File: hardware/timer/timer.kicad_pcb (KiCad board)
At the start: 2 copper layers, 80 x 80 mm, 22 parts, among them J1 JST_XH_HOST_UART, U1 Pico, U2 TM1637

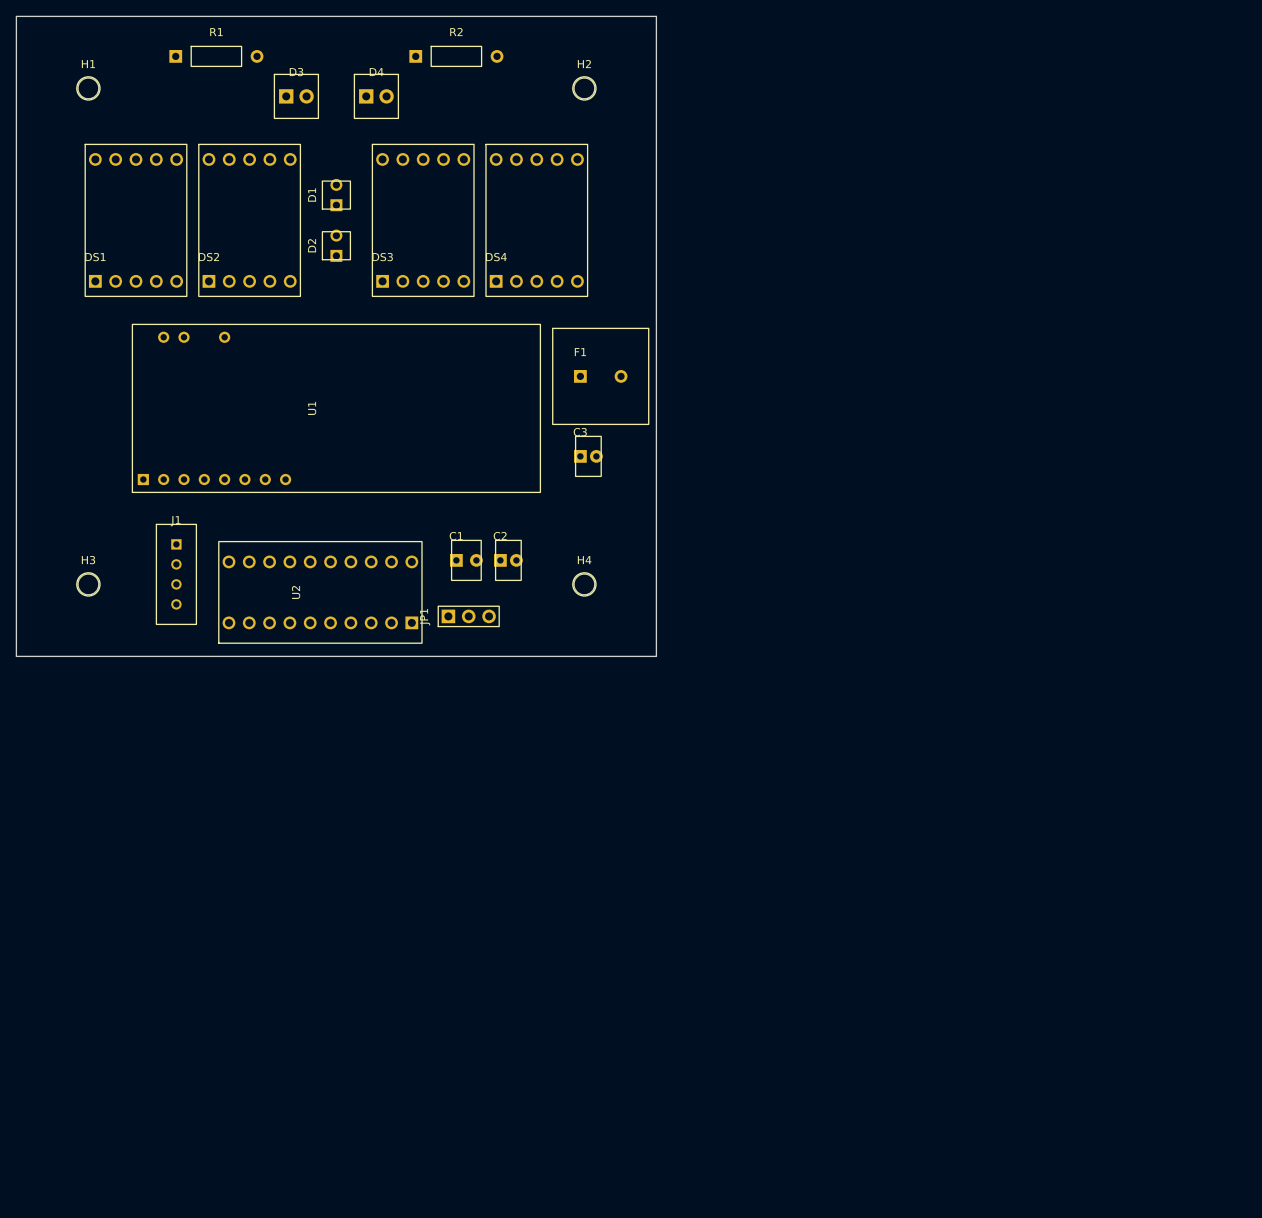
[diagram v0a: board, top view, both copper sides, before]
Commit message: タイマー基板: 実フットプリント化・電池入力(J6/Q1/R5)追加・Pico 40ピン化・配線
- PCBを実ライブラリのフットプリントで作り直し、以後KiCadで手編集(tools/に一回限りのスクリプト)
- 回路図のFootprintフィールドを補完、C3を8mm缶に変更
- Pico専用フットプリント RPi_Pico_TH_Headers(THT40ピンのみ、浮き実装、3D +2.5mm)と40ピンシンボル
- 電池入力 J6 -> Q1(逆接続保護) -> +5V。F6は廃止(保護は電池箱側)
- 未解決(作業途中): DRCのstarved_thermal 4件、回路図とのパリティ差分(基板更新で解消見込み)

Co-Authored-By: Claude Sonnet 5.5 <noreply@anthropic.com>
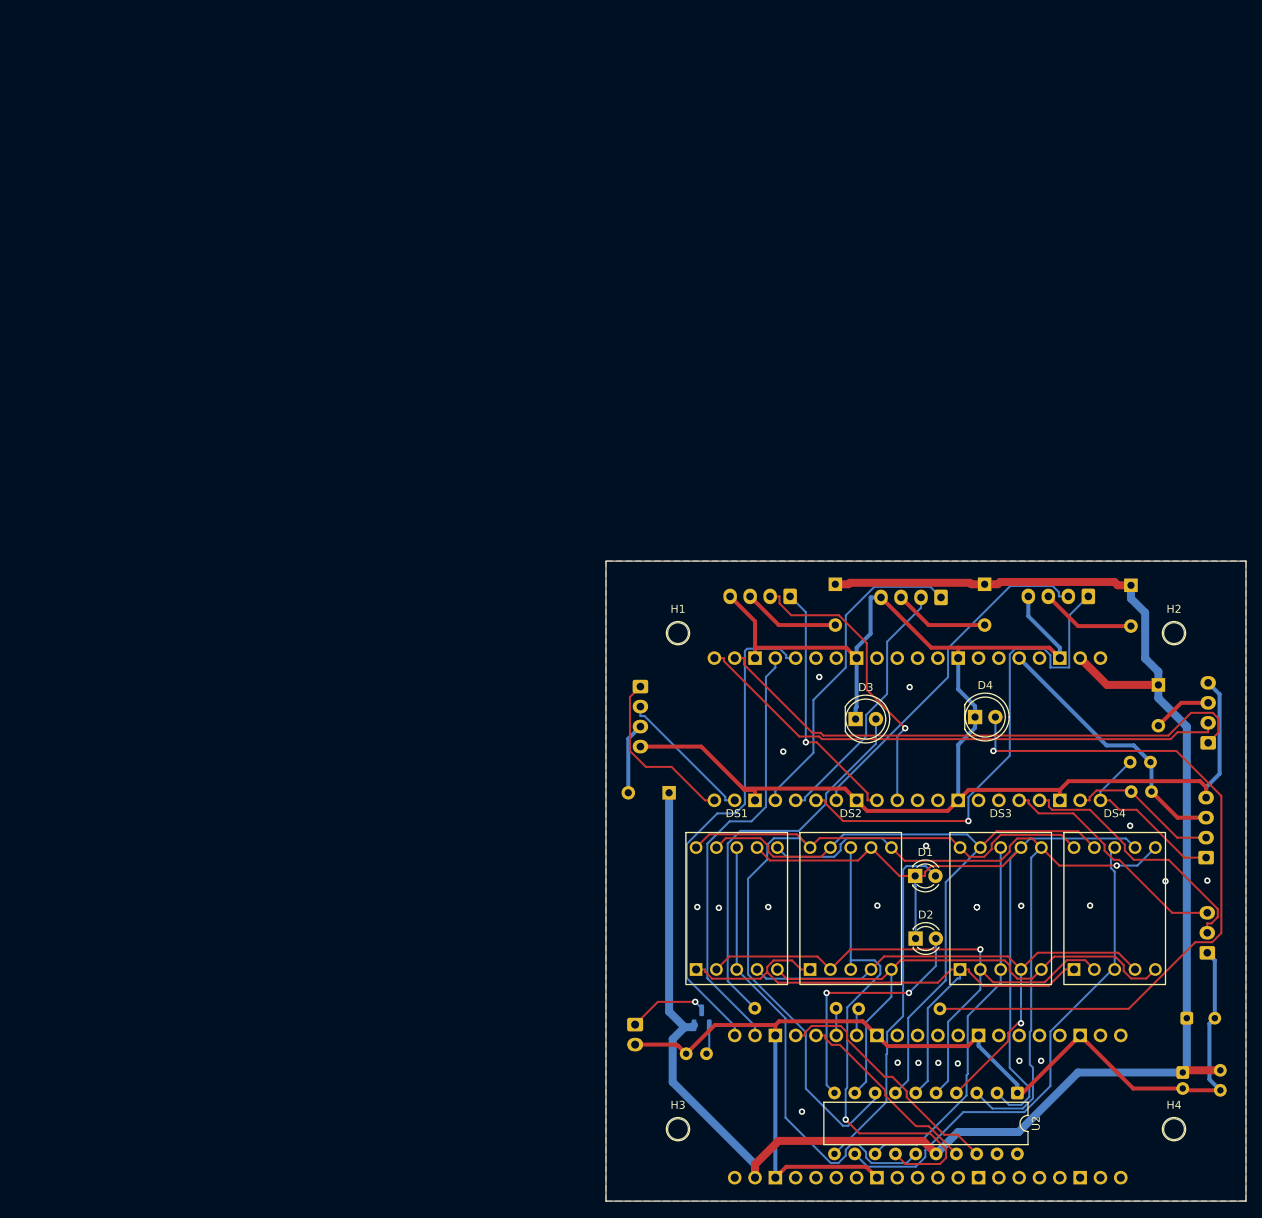
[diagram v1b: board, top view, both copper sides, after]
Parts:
- removed JP1: TM1637_VDD_SEL, Connector_PinHeader_2.54mm:PinHeader_1x03_P2.54mm_Vertical
- added F2: MF-RX030/72-0 (0.3A hold, Akizuki 113076), Timer_Local:MF-RX030_Radial_P5.10mm, B.Cu at (121.0, 71.0)
- added F3: MF-RX030/72-0 (0.3A hold, Akizuki 113076), Timer_Local:MF-RX030_Radial_P5.10mm, B.Cu at (139.3, 71.1)
- added F4: MF-RX030/72-0 (0.3A hold, Akizuki 113076), Timer_Local:MF-RX030_Radial_P5.10mm, B.Cu at (81.6, 97.0)
- added F5: MF-RX030/72-0 (0.3A hold, Akizuki 113076), Timer_Local:MF-RX030_Radial_P5.10mm, B.Cu at (142.7, 83.6)
- added J2: MODULE_SLOT_2, Connector_JST:JST_XH_B4B-XH-A_1x04_P2.50mm_Vertical, B.Cu at (115.6, 72.6)
- added J3: MODULE_SLOT_3, Connector_JST:JST_XH_B4B-XH-A_1x04_P2.50mm_Vertical, B.Cu at (134.0, 72.5)
- added J4: MODULE_SLOT_4, Connector_JST:JST_XH_B4B-XH-A_1x04_P2.50mm_Vertical, B.Cu at (78.0, 83.8)
- added J5: MODULE_SLOT_5, Connector_JST:JST_XH_B4B-XH-A_1x04_P2.50mm_Vertical, B.Cu at (149.0, 90.8)
- added J6: PWR_IN, Connector_JST:JST_XH_B2B-XH-A_1x02_P2.50mm_Vertical, B.Cu at (77.3, 126.0)
- added J7: SHARED_WIDGET_I2C_TAP, Connector_JST:JST_XH_B4B-XH-A_1x04_P2.50mm_Vertical, B.Cu at (148.7, 105.2)
- added J8: SHARED_WIDGET_GPIO, Connector_JST:JST_XH_B3B-XH-A_1x03_P2.50mm_Vertical, B.Cu at (148.9, 117.1)
- added Q1: IRLML6402, Package_TO_SOT_SMD:SOT-23, B.Cu at (85.7, 125.2)
- added R3: 4.7k, Resistor_THT:R_Axial_DIN0207_L6.3mm_D2.5mm_P2.54mm_Vertical, B.Cu at (141.8, 93.2)
- added R4: 4.7k, Resistor_THT:R_Axial_DIN0207_L6.3mm_D2.5mm_P2.54mm_Vertical, B.Cu at (141.9, 96.9)
- added R5: 100k, Resistor_THT:R_Axial_DIN0207_L6.3mm_D2.5mm_P2.54mm_Vertical, B.Cu at (86.3, 129.7)
- added U3: Pico 2 (host / communication), Timer_Local:RPi_Pico_TH_Headers, B.Cu at (111.4, 89.1)
- C1, C2, R1, R2: moved to B.Cu
- C3: value 100uF -> 470uF; footprint Capacitor_THT:CP_Radial_D5.0mm_P2.00mm -> Capacitor_THT:CP_Radial_D8.0mm_P3.50mm; moved to B.Cu
- D1: value LED -> LED (colon, top)
- D2: value LED -> LED (colon, bottom)
- D3: value LED -> LED (strike 1)
- D4: value LED -> LED (strike 2)
- F1: value MF-R185 -> MF-RX030/72-0 (0.3A hold, Akizuki 113076); footprint Fuse_THT:Fuse_Radial_D12.0mm_P5.08mm -> Timer_Local:MF-RX030_Radial_P5.10mm; moved to B.Cu
- J1: value JST_XH_HOST_UART -> MODULE_SLOT_1; moved to B.Cu
- U1: footprint RPi_Pico:RPi_Pico_SMD_TH -> Timer_Local:RPi_Pico_TH_Headers; moved to B.Cu
- U2: footprint Timer_Local:TM1637 -> Package_DIP:DIP-20_W7.62mm
- moved R1 142.0 mm to (102.5, 124.0), turned to 180 degrees
- moved R2 129.2 mm to (105.3, 124.1)
- moved C1 114.8 mm to (150.5, 131.7), turned to -90 degrees
- moved U1 114.4 mm to (113.9, 136.3), turned to -90 degrees
- moved DS2 114.2 mm to (99.2, 119.1)
- moved DS1 114.2 mm to (85.0, 119.1)
- moved D2 112.9 mm to (112.4, 115.3), turned to 0 degrees
- moved DS4 112.3 mm to (132.2, 119.1)
- moved DS3 112.3 mm to (118.0, 119.1)
- moved D1 111.7 mm to (112.3, 107.4), turned to 0 degrees
- moved D4 107.8 mm to (119.8, 87.6)
- moved U2 107.3 mm to (125.1, 134.6), turned to -90 degrees
- moved C2 106.6 mm to (145.8, 132.0), turned to -90 degrees
- moved D3 104.6 mm to (104.9, 87.8)
- moved C3 103.3 mm to (146.3, 125.2)
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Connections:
- net GRID_COLON1 renamed /GRID_COLON1
- net GRID_COLON2 renamed /GRID_COLON2
- net GRID_D1 renamed /GRID_D1
- net GRID_D2 renamed /GRID_D2
- net GRID_D3 renamed /GRID_D3
- net GRID_D4 renamed /GRID_D4
- net SEG_A renamed /SEG_A
- net SEG_B renamed /SEG_B
- net SEG_C renamed /SEG_C
- net SEG_D renamed /SEG_D
- net SEG_DP renamed /SEG_DP
- net SEG_E renamed /SEG_E
- net SEG_F renamed /SEG_F
- net SEG_G renamed /SEG_G
- net STRIKE1 renamed /STRIKE1
- net STRIKE1_LED renamed /STRIKE1_LED
- net STRIKE2 renamed /STRIKE2
- net STRIKE2_LED renamed /STRIKE2_LED
- net TM_CLK renamed /TM_CLK
- net TM_DIO renamed /TM_DIO
- C1 pad 1: TM_VDD -> +5V
- C2 pad 1: TM_VDD -> +5V
- C3 pad 1: J1_5V -> +5V
- F1 pad 2: J1_5V -> /VCC_J1
- J1 pad 1: UART_TX -> /S1_RX
- J1 pad 2: UART_RX -> /S1_TX
- J1 pad 3: J1_5V -> /VCC_J1
- U1 pad 1: UART_TX -> /M_RX
- U1 pad 2: UART_RX -> /M_TX
- U1 pad 36: +3V3 -> +3.3V
- U2 pad 16: TM_VDD -> +5V
- U2 pad 19: (no net) -> unconnected-(U2-K1-Pad19)
- U2 pad 20: (no net) -> unconnected-(U2-K2-Pad20)
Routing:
- net GND: track 0.00 -> 330.9 mm, vias 0 -> 21
- net +5V: track 0.00 -> 233.7 mm
- net /SEG_G: track 0.00 -> 105.6 mm
- net /SEG_A: track 0.00 -> 98.4 mm
- net /SEG_B: track 0.00 -> 94.7 mm, vias 0 -> 1
- net /STRIKE2_LED: track 0.00 -> 91.9 mm, vias 0 -> 1
- net /SEG_F: track 0.00 -> 87.7 mm
- net /SEG_E: track 0.00 -> 76.0 mm
- net /SEG_D: track 0.00 -> 72.2 mm, vias 0 -> 1
- net /SEG_DP: track 0.00 -> 70.6 mm
- net /SEG_C: track 0.00 -> 70.3 mm, vias 0 -> 1
- net /S5_RX: track 0.00 -> 70.0 mm
- net /S5_TX: track 0.00 -> 67.7 mm
- net /GRID_D4: track 0.00 -> 63.5 mm
- net /S3_RX: track 0.00 -> 62.8 mm, vias 0 -> 1
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- added copper zone on B.Cu, net GND
- added copper zone on F.Cu, net GND
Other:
- board text added: "PROVISIONAL: 80x80mm, two Pico 2 (U1 timer, U3 host), dual-sided: front = display + Picos (pin-header mounted), back = JST/fuses/TM1637/passives; 4x M2.6 holes (9mm inset); dashed 12mm squares = corner keep-out (hub 2026-09-29)"
- board text removed: "PROVISIONAL: 80x80mm outline; 4x M2.6 mounting holes placed per 2026-09-29 hub decision (dia 2.6mm, 9mm inset from edge); dashed 15mm squares = corner keep-out (kept conservative pending screw head/washer confirmation)"

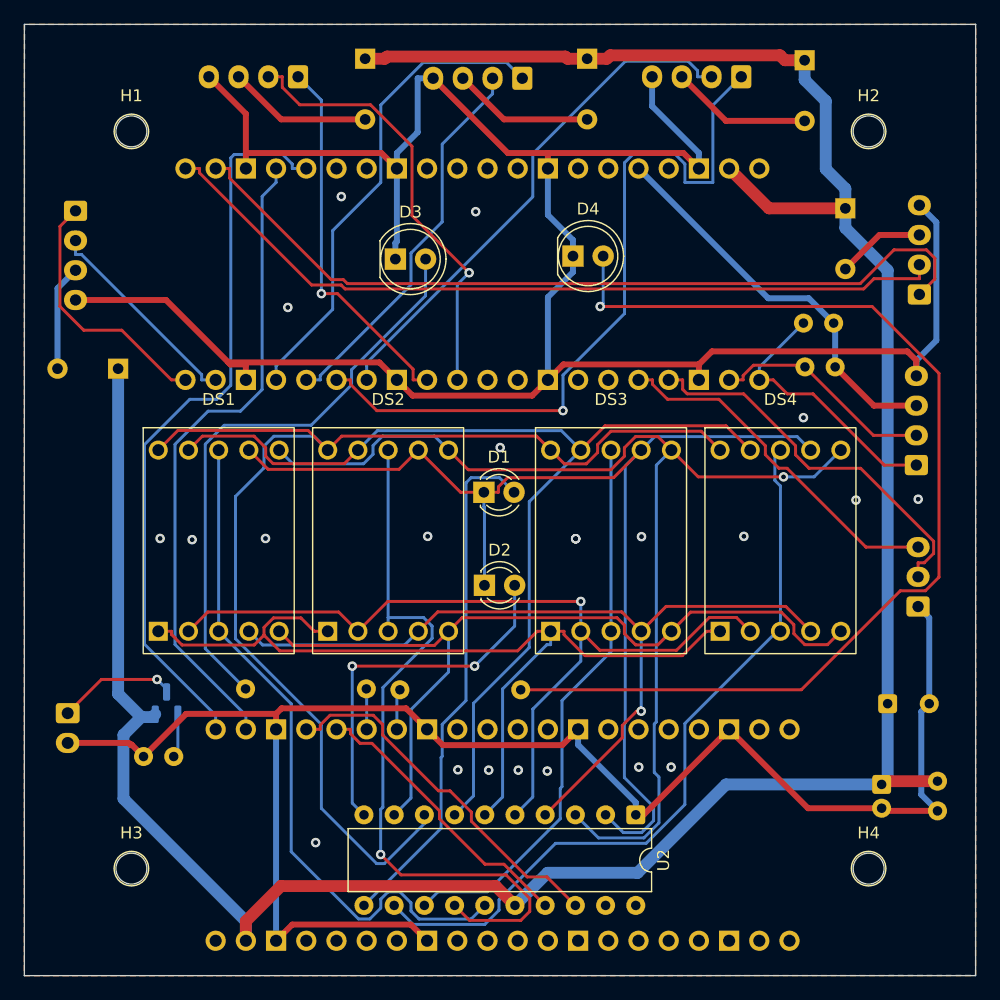
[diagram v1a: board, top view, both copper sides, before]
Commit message: タイマー基板: 電池入力にDC-DC(AE-TPS63802)を追加、F6復活、共有ライブラリ(shared_lib)
- 電池(単3x3)J6 -> F6 -> Q1(逆接続保護) -> AE-TPS63802(昇降圧) -> +5V
- Timer_Local に AE-TPS63802 のシンボル/フットプリントを追加
- hardware/shared_lib: OSC_Shared(Pico_TH40、RPi_Pico_TH_Headers)と適用スクリプト
- 回路図とPCBのパリティ0

作業途中(未解決): DRCのitems_not_allowed 7件(+5V/VBAT_Fの配線端点が隅12mm角に入る)、starved_thermal 10件

Co-Authored-By: Claude Sonnet 5.5 <noreply@anthropic.com>
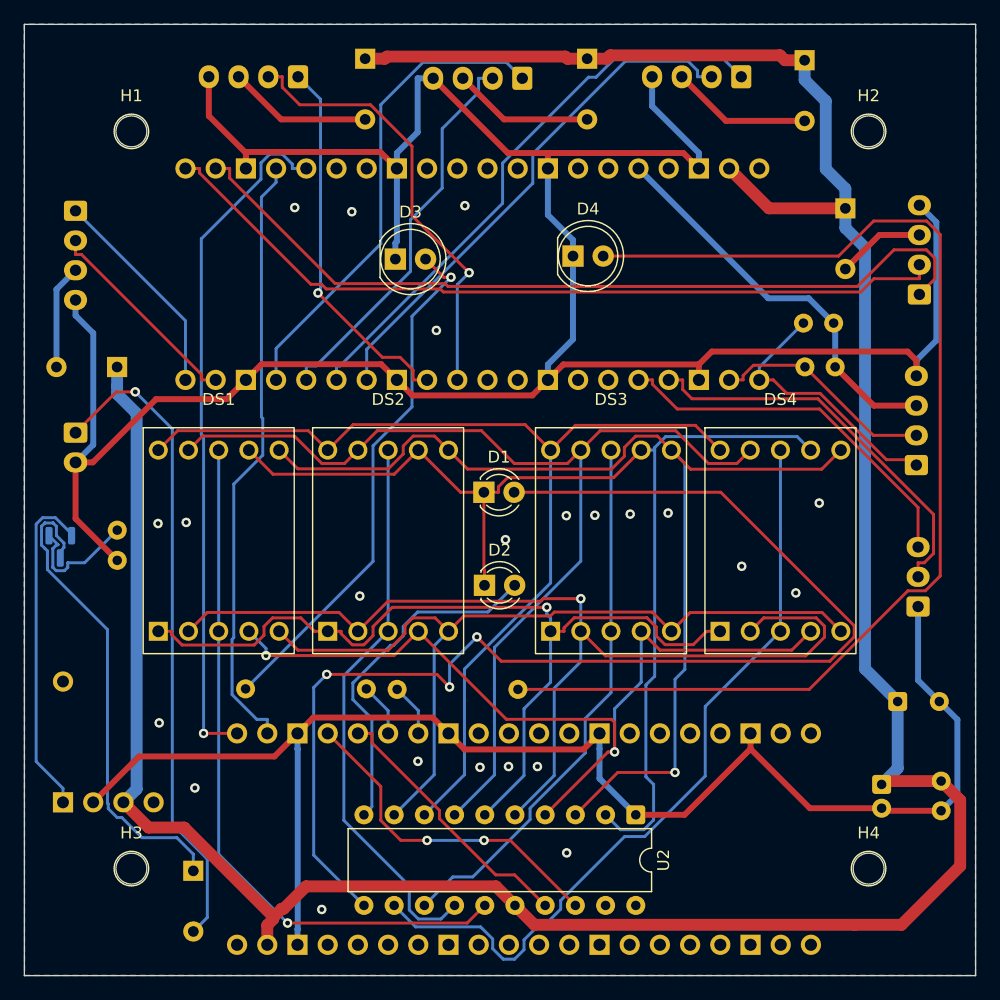
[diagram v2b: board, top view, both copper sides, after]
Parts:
- added F6: Polyfuse_Small, Timer_Local:MF-R185_Radial_P5.10mm, B.Cu at (87.9, 139.3)
- added U4: AE-TPS63802, Timer_Local:AE-TPS63802, B.Cu at (77.0, 133.5)
- C1: value 100nF -> C
- C2: value 100uF -> C_Polarized
- C3: value 470uF -> C_Polarized
- D1: value LED (colon, top) -> LED
- D2: value LED (colon, bottom) -> LED
- D3: value LED (strike 1) -> LED
- D4: value LED (strike 2) -> LED
- F1, F2, F3, F4, F5: value MF-RX030/72-0 (0.3A hold, Akizuki 113076) -> Polyfuse_Small
- J1: value MODULE_SLOT_1 -> Conn_01x04
- J2: value MODULE_SLOT_2 -> Conn_01x04
- J3: value MODULE_SLOT_3 -> Conn_01x04
- J4: value MODULE_SLOT_4 -> Conn_01x04
- J5: value MODULE_SLOT_5 -> Conn_01x04
- J6: value PWR_IN -> Conn_01x02
- J7: value SHARED_WIDGET_I2C_TAP -> Conn_01x04
- J8: value SHARED_WIDGET_GPIO -> Conn_01x03
- R1, R2: value 330 -> R
- R3, R4: value 4.7k -> R
- R5: value 100k -> R
- U3: value Pico 2 (host / communication) -> Pico
- moved J6 23.6 mm to (78.0, 102.4)
- moved R5 19.6 mm to (81.5, 110.6), turned to -90 degrees
- moved Q1 15.9 mm to (76.7, 112.0), turned to -90 degrees
- moved U1 1.83 mm to (115.7, 136.6)
- moved C3 0.86 mm to (147.1, 125.0)
- moved C1 0.31 mm to (150.8, 131.7)
- moved R2 0.24 mm to (105.0, 124.0)
- moved F4 0.16 mm to (81.5, 96.9)
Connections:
- J6 pad 1: /VIN_5V -> Net-(J6-Pin_1)
- Q1 pad 2: +5V -> /VIN_DCDC
- Q1 pad 3: /VIN_5V -> /VBAT_F
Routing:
- net /GRID_COLON1: track 43.8 -> 105.2 mm, vias 0 -> 3
- net Net-(J6-Pin_1): track 0.00 -> 54.8 mm, vias 0 -> 1
- net /VBAT_F: track 0.00 -> 40.7 mm
- net /VIN_DCDC: track 0.00 -> 28.3 mm
- net /SEG_G: track 105.6 -> 87.2 mm
- net /GRID_D2: track 62.6 -> 47.1 mm, vias 1 -> 0
- net /S3_RX: track 62.8 -> 48.7 mm, vias 1 -> 0
- net /SEG_D: track 72.2 -> 85.8 mm
- net +5V: track 233.7 -> 245.3 mm
- net /VIN_5V: track 10.1 -> 0.00 mm, vias 1 -> 0
- net GND: track 330.9 -> 338.8 mm, vias 21 -> 23
- net Net-(Q1-G): track 3.70 -> 10.4 mm
- net /STRIKE2_LED: track 91.9 -> 98.2 mm, vias 1 -> 0
- net /STRIKE1_LED: track 49.5 -> 44.5 mm, vias 0 -> 1
- net /M_RX: track 62.0 -> 57.8 mm, vias 0 -> 1
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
